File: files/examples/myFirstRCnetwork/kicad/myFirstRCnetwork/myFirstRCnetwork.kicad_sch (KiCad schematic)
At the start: 6 parts

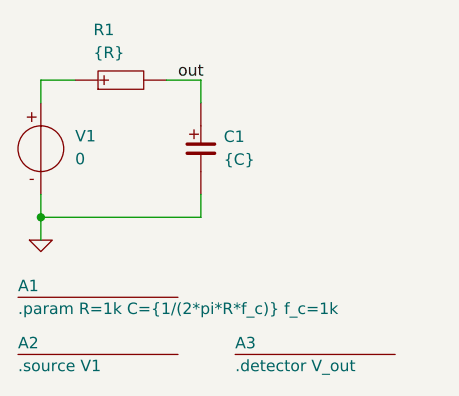
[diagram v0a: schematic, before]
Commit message: Updated jupyter notebook interface
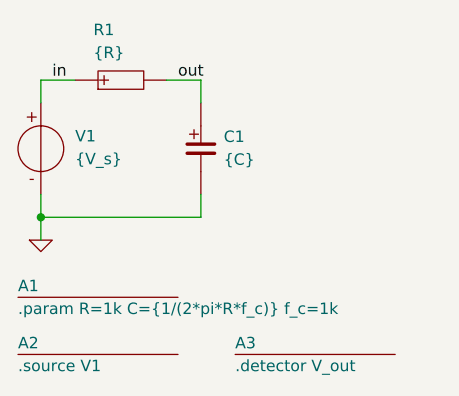
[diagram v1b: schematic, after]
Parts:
- V1: value 0 -> {V_s}
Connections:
- net in: now reaches R1.2, V1.1 (p)
